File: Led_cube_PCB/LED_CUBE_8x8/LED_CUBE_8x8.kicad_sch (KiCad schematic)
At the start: 27 parts, among them IC1 74LVC244APW,118, IC10 74LVC244APW,118, IC11 74LVC244APW,118, IC12 74LVC244APW,118, IC13 74LVC244APW,118, IC14 74LVC244APW,118, IC15 74LVC244APW,118, IC16 74LVC244APW,118, IC17 74LVC244APW,118, IC18 74LVC244APW,118, IC19 74LVC244APW,118, IC2 74LVC244APW,118, IC20 74LVC244APW,118, IC21 74LVC244APW,118, IC22 74LVC244APW,118, IC23 74LVC244APW,118, IC24 74LVC244APW,118, IC25 74AHC138PW,118, IC26 74AHC138PW,118, IC27 74AHC138PW,118, IC3 74LVC244APW,118, IC4 74LVC244APW,118, IC5 74LVC244APW,118, IC6 74LVC244APW,118, IC7 74LVC244APW,118, IC8 74LVC244APW,118, IC9 74LVC244APW,118

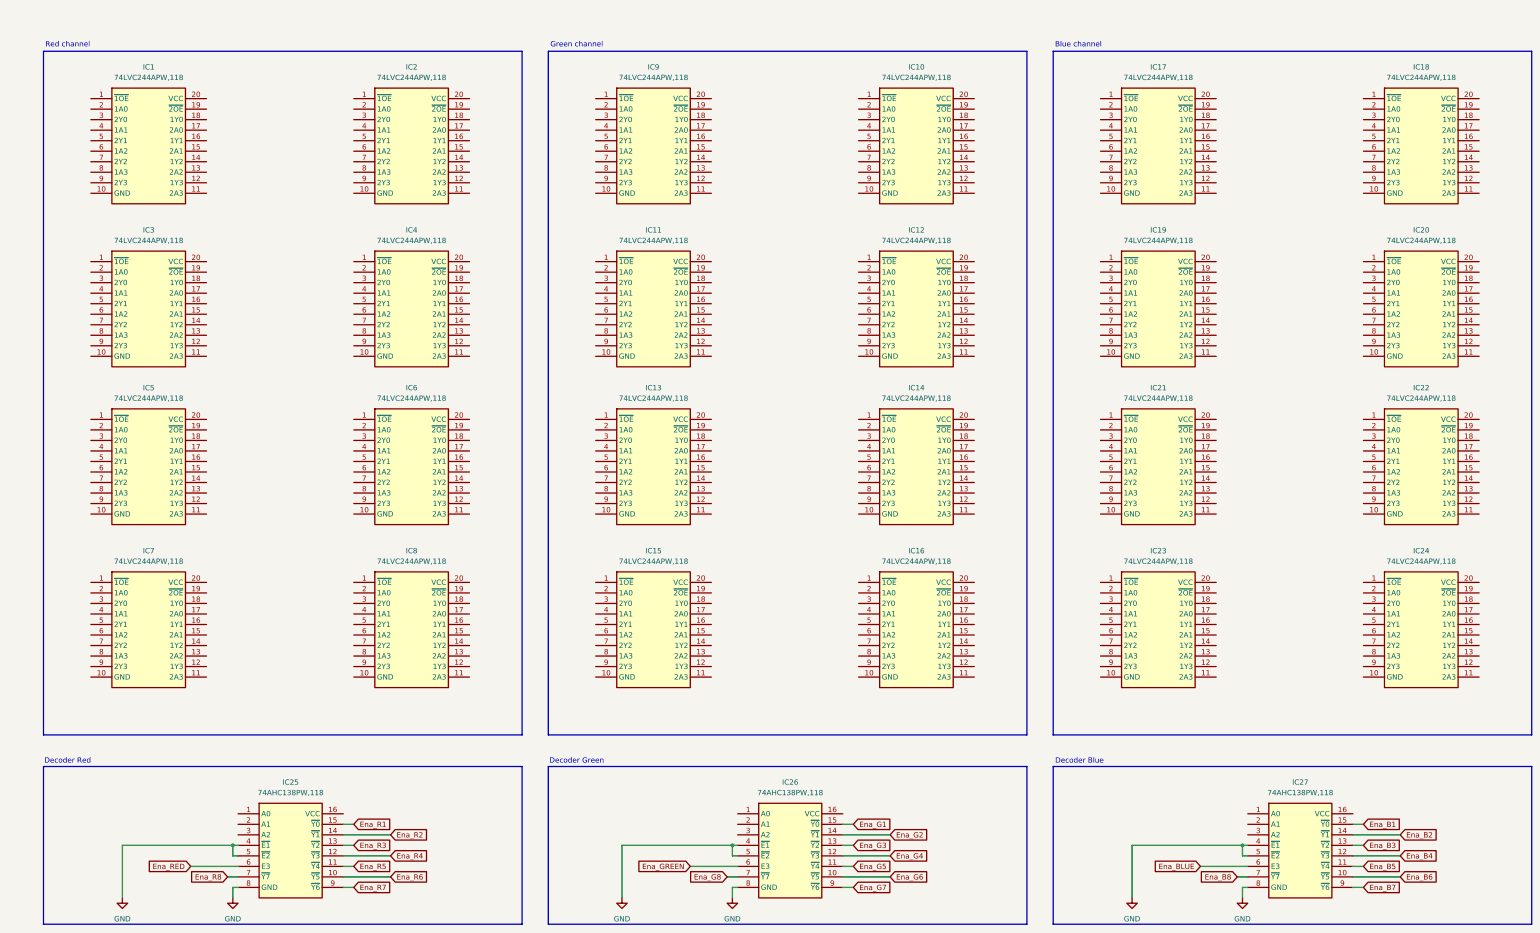
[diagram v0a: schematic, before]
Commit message: changed buffer to a 5V tolerant one and worked on the schematic.
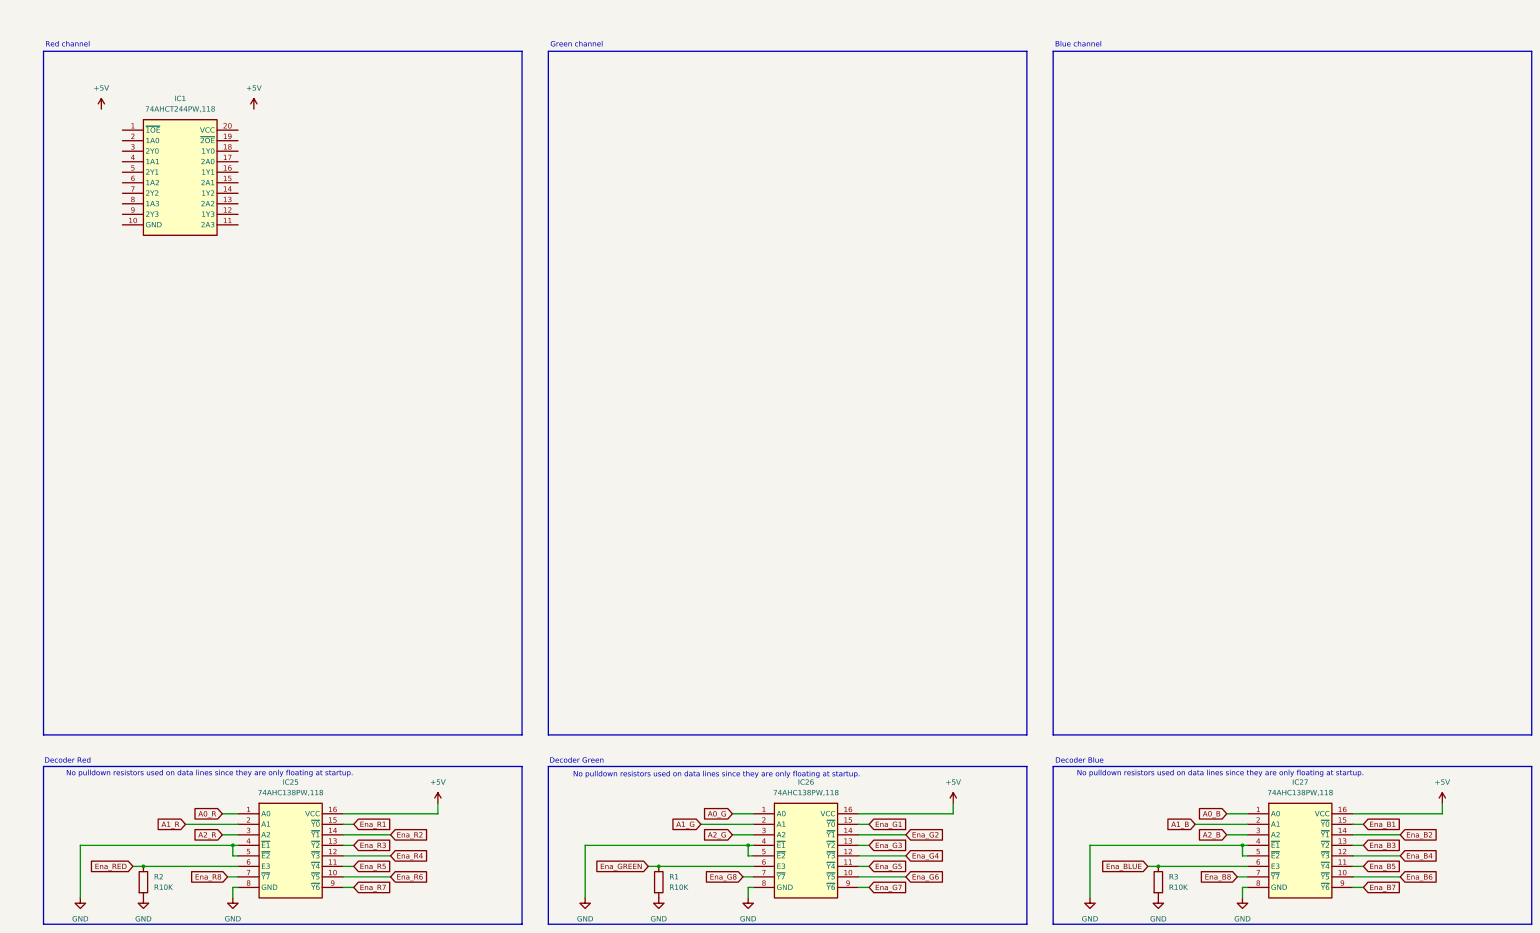
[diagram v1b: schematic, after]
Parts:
- removed IC1, IC10, IC11, IC12, IC13, IC14, IC15, IC16, IC17, IC18, IC19, IC2, IC20, IC21, IC22, IC23, IC24, IC3, IC4, IC5, IC6, IC7, IC8, IC9: 74LVC244APW,118, SOP65P640X110-20N, symbol SamacSys_Parts:74LVC244APW,118
- added IC1: 74AHCT244PW,118, SOP65P640X110-20N, symbol SamacSys_Parts:74AHCT244PW,118
- added R1, R2, R3: R10K, symbol Device:R
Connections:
- net Ena_BLUE: now also R3.1
- net Ena_GREEN: now also R1.1
- net Ena_RED: now also R2.1
- net GND: now also R1.2, R2.2, R3.2
- net A0_B: now reaches IC27.1 (A0)
- net +5V: now reaches IC27.16 (VCC)
- net +5V: now also IC25.16 (VCC), IC26.16 (VCC)
- net A1_B: now reaches IC27.2 (A1)
- net A2_B: now reaches IC27.3 (A2)
- net A0_G: now reaches IC26.1 (A0)
- net A1_G: now reaches IC26.2 (A1)
- net A2_G: now reaches IC26.3 (A2)
- net A0_R: now reaches IC25.1 (A0)
- net A1_R: now reaches IC25.2 (A1)
- net A2_R: now reaches IC25.3 (A2)
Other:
- note added: "No pulldown resistors used on data lines since they are only floating at startup."
- moved on the sheet: IC26

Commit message: Made progress on schematic red channel multiplexing almost finished.
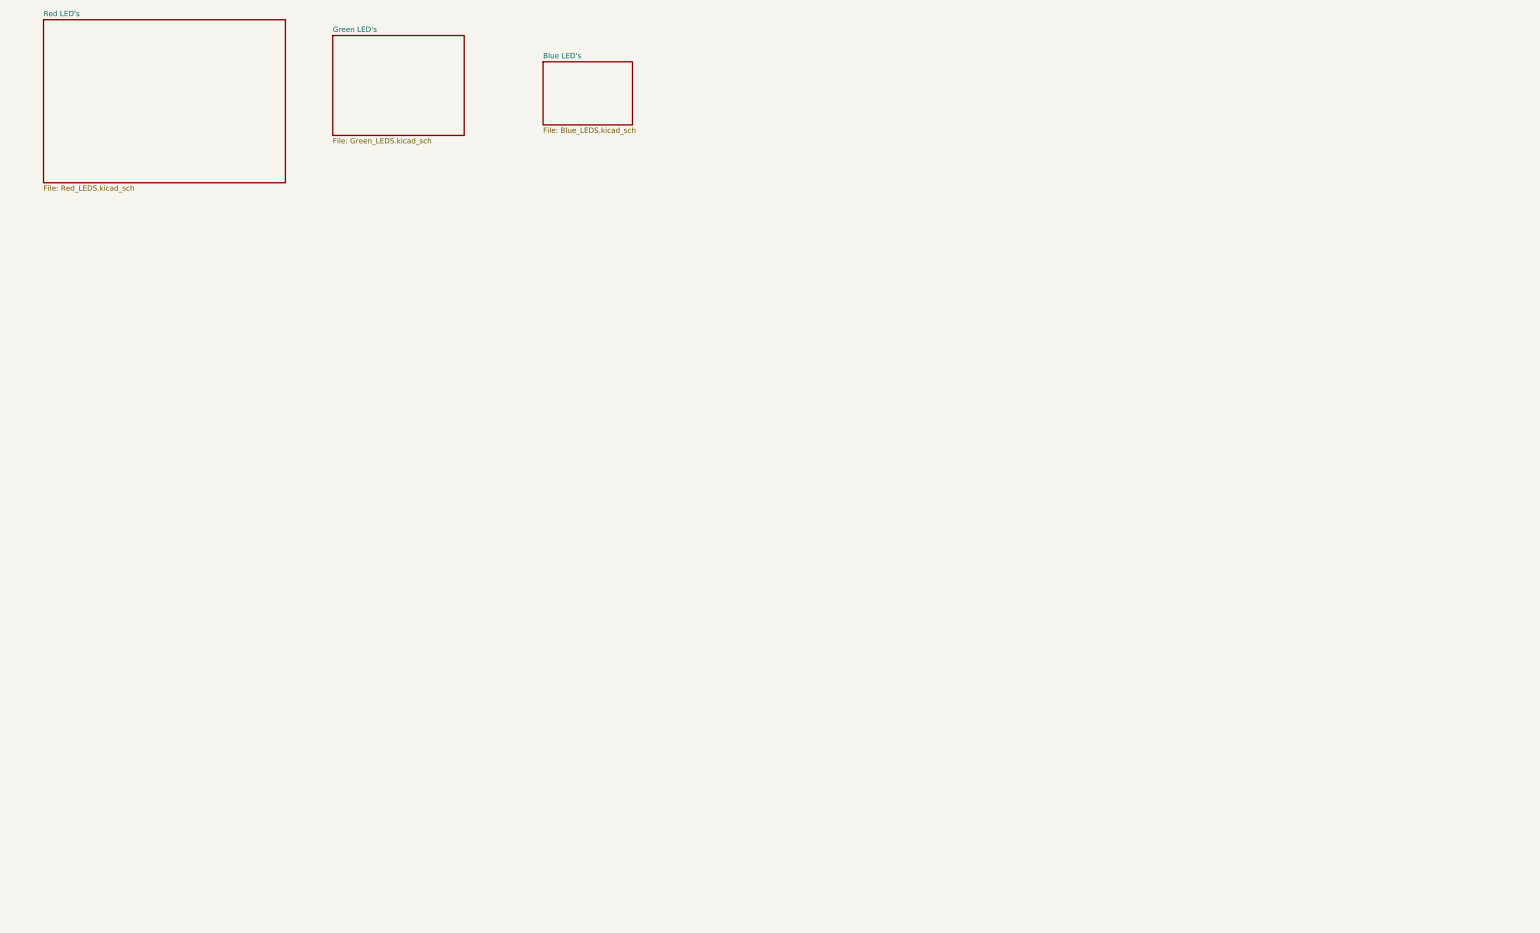
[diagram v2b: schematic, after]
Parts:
- removed IC1: 74AHCT244PW,118, SOP65P640X110-20N, symbol SamacSys_Parts:74AHCT244PW,118
- removed IC25, IC26, IC27: 74AHC138PW,118, SOP65P640X110-16N, symbol SamacSys_Parts:74AHC138PW,118
- removed R1, R2, R3: R10K, symbol Device:R
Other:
- added sheet Blue LED's (Blue_LEDS.kicad_sch)
- added sheet Green LED's (Green_LEDS.kicad_sch)
- added sheet Red LED's (Red_LEDS.kicad_sch)
- note removed: "Blue channel"
- note removed: "Decoder Blue"
- note removed: "Decoder Green"
- note removed: "Decoder Red"
- note removed: "Green channel"
- note removed: "No pulldown resistors used on data lines since they are only floating at startup."
- note removed: "Red channel"

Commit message: Finished the schematic for the red green and blue color multiplexing.
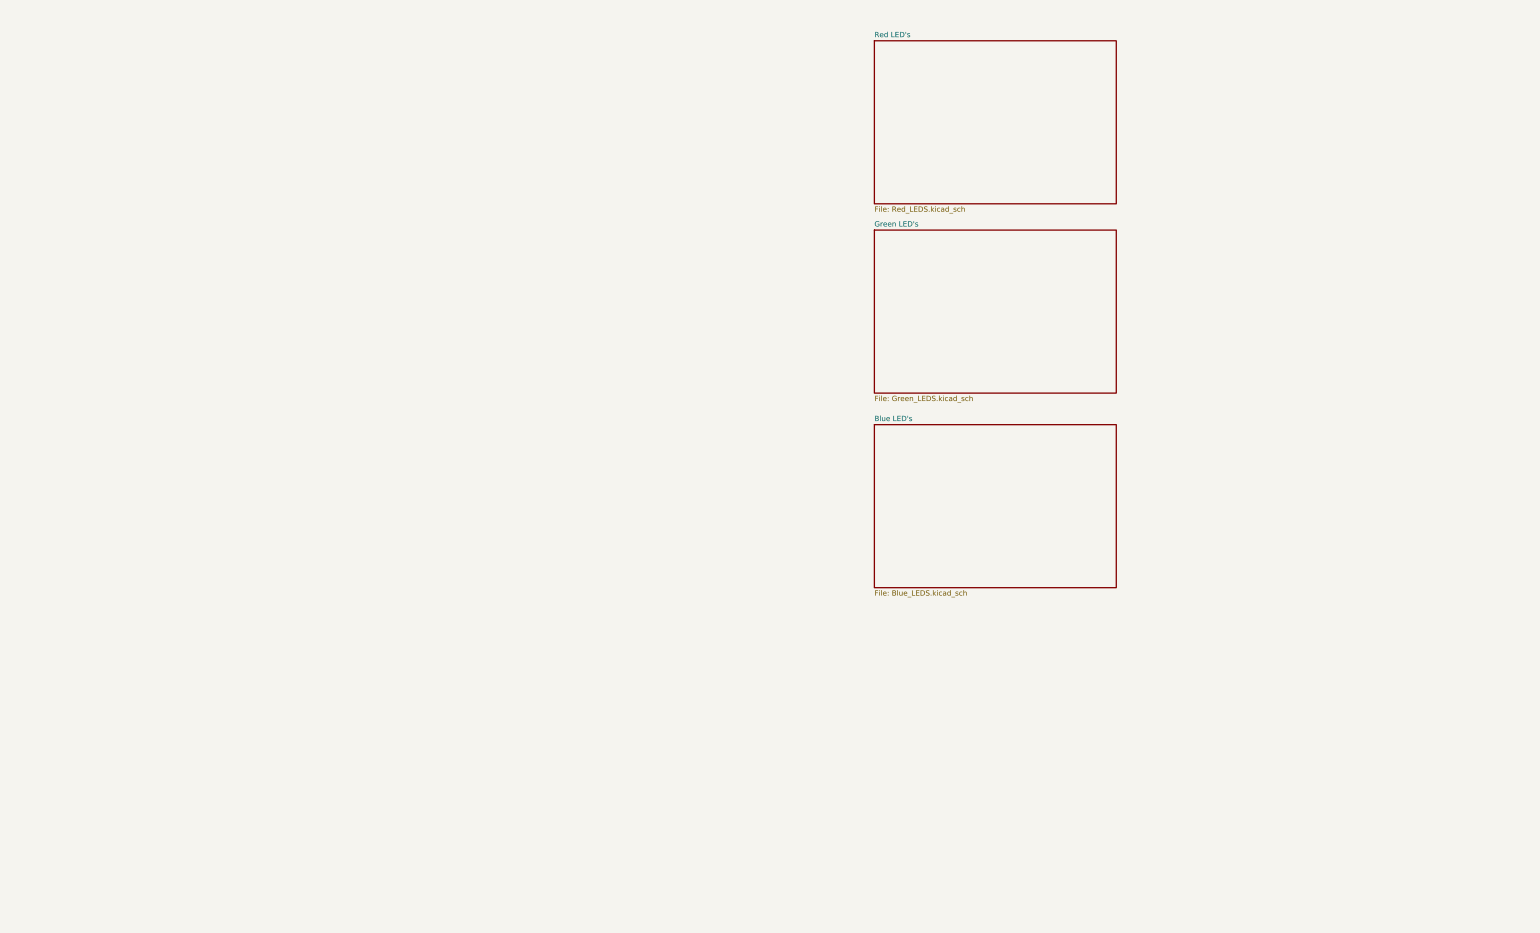
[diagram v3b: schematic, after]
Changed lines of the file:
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@@
 	)
 	(sheet
-		(at 92.71 22.86)
-		(size 31.75 24.13)
+		(at 223.52 69.85)
+		(size 58.42 39.37)
 		(exclude_from_sim no)
 		(in_bom yes)
@@
 		)
 		(property "Sheetname" "Green LED's"
-			(at 92.71 22.1484 0)
+			(at 223.52 69.1384 0)
 			(effects
 				(font
@@
 		)
 		(property "Sheetfile" "Green_LEDS.kicad_sch"
-			(at 92.71 47.5746 0)
+			(at 223.52 109.8046 0)
 			(effects
 				(font
@@
 	)
 	(sheet
-		(at 22.86 19.05)
+		(at 223.52 24.13)
 		(size 58.42 39.37)
 		(exclude_from_sim no)
@@
 		)
 		(property "Sheetname" "Red LED's"
-			(at 22.86 18.3384 0)
+			(at 223.52 23.4184 0)
 			(effects
 				(font
@@
 		)
 		(property "Sheetfile" "Red_LEDS.kicad_sch"
-			(at 22.86 59.0046 0)
+			(at 223.52 64.0846 0)
 			(effects
 				(font
@@
 	)
 	(sheet
-		(at 143.51 29.21)
-		(size 21.59 15.24)
+		(at 223.52 116.84)
+		(size 58.42 39.37)
 		(exclude_from_sim no)
 		(in_bom yes)
@@
 		)
 		(property "Sheetname" "Blue LED's"
-			(at 143.51 28.4984 0)
+			(at 223.52 116.1284 0)
 			(effects
 				(font
@@
 		)
 		(property "Sheetfile" "Blue_LEDS.kicad_sch"
-			(at 143.51 45.0346 0)
+			(at 223.52 156.7946 0)
 			(effects
 				(font

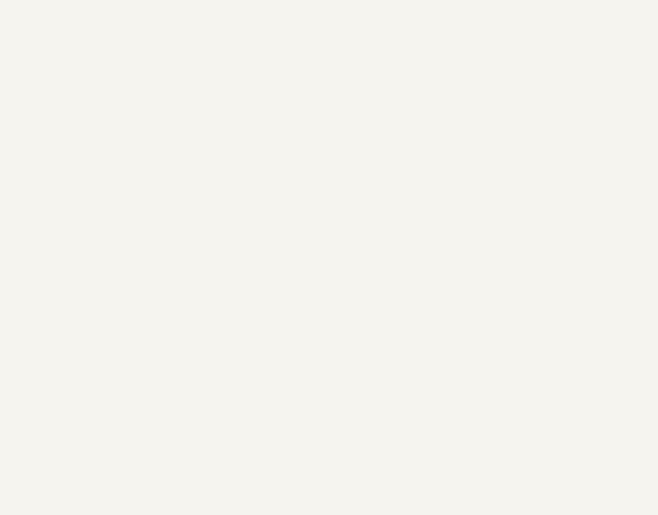
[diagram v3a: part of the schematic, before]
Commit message: added power schematic and updated labels to correct type e.g. output, input
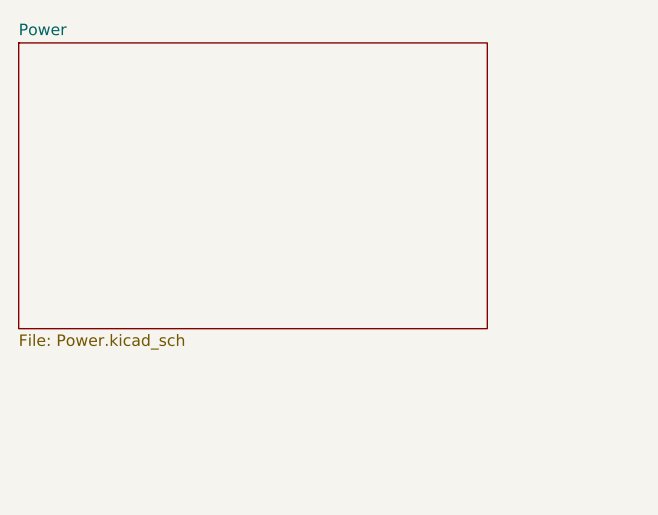
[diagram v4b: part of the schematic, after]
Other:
- added sheet Power (Power.kicad_sch)
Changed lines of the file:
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@@
+		)
+	)
+	(sheet
+		(at 21.59 22.86)
+		(size 52.07 31.75)
+		(exclude_from_sim no)
+		(in_bom yes)
+		(on_board yes)
+		(dnp no)
+		(fields_autoplaced yes)
+		(stroke
+			(width 0.1524)
+			(type solid)
+		)
+		(fill
+			(color 0 0 0 0.0000)
+		)
+		(property "Sheetname" "Power"
+			(at 21.59 22.1484 0)
+			(effects
+				(font
+					(size 1.27 1.27)
+				)
+				(justify left bottom)
+			)
+		)
+		(property "Sheetfile" "Power.kicad_sch"
+			(at 21.59 55.1946 0)
+			(effects
+				(font
+					(size 1.27 1.27)
+				)
+				(justify left top)
+			)
+		)
+		(instances
+			(project "LED_CUBE_8x8"
+				(path "/b239677e-e361-4439-8200-63fb41f7e03c"
+					(page "5")
+				)
+			)
 		)
 	)
